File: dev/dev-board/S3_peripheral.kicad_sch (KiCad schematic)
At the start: 0 parts

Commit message: making CAD
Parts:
- added C10, C13, C15, C16, C17, C18, C9: 0.1uF, Capacitor_SMD:C_0603_1608Metric, symbol Device:C
- added C14: 120uF, easyeda2kicad:CAP-SMD_BD8.0-L8.3-W8.3-RD, symbol Device:C_Polarized
- added C19: 10uF, Capacitor_SMD:C_0603_1608Metric, symbol Device:C
- added Card1: TF PUSH, easyeda2kicad:TF-SMD_TF-PUSH, symbol easyeda2kicad:TFPUSH
- added D1: LED GREEN, LED_SMD:LED_0805_2012Metric, symbol Device:LED
- added LED1: TSOP38238, easyeda2kicad:SENSOR-TG_TSOP38236, symbol easyeda2kicad:TSOP38238
- added P1: HDR-IDC-2.54-2X5P, easyeda2kicad:IDC-TH_10P-P2.54_C5665, symbol easyeda2kicad:HDR-IDC-2.54-2X5P
- added R13, R14, R15, R16, R17, R18, R20, R21, R22, R23, R24, R25, R26: 10K, Resistor_SMD:R_0603_1608Metric, symbol Device:R
- added R19: 1K, Resistor_SMD:R_0603_1608Metric, symbol Device:R
- added R27: 22, Resistor_SMD:R_0603_1608Metric, symbol Device:R
- added SW6, SW7, SW8, SW9: TSC015A03526A, easyeda2kicad:SW-SMD_4P-L4.5-W4.5-P3.00-LS6.8, symbol easyeda2kicad:TSC015A03526A
- added U10: TPS2065CDBV, Package_TO_SOT_SMD:SOT-23-5, symbol Power_Management:TPS2065CDBV
- added U11: PESD5V0U2BT, easyeda2kicad:SOT-23-3_L2.9-W1.3-P1.90-LS2.4-BR, symbol easyeda2kicad:PESD5V0U2BT
- added U12: PESD5V0S1BA_C5261083, easyeda2kicad:SOD-323_L1.7-W1.3-LS2.5-BI, symbol easyeda2kicad:PESD5V0S1BA_C5261083
- added U8, U9: ZX-HY2.0-4PWZ, easyeda2kicad:CONN-TH_4P-P2.00_ZX-HY2.0-4PWZ, symbol easyeda2kicad:ZX-HY2.0-4PWZ
- added USB2: USB-231-ARY, easyeda2kicad:USB-A-TH_USB-231-ARY, symbol easyeda2kicad:USB-231-ARY
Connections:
- new net: R18.2, U10.3 (~{FLT})
- new net: D1.2 (A), R19.1
- new net: C14.1, C16.1, U10.1 (OUT), U12.1, USB2.1 (VBUS)
- new net: Card1.5 (CLX), R27.2
- new net +3V3: C17.2, C18.1, C19.1, C9.2, Card1.4 (VDD), LED1.3 (VS), P1.4, R13.2, R14.2, R15.2, R16.2, R20.1, R21.2, R22.2, R23.2, R24.2, R25.1, R26.2
- new net ButtonCancel: R24.1, SW7.1, SW7.2
- new net ButtonDown: R22.1, SW8.1, SW8.2
- new net ButtonEnter: R23.1, SW9.1, SW9.2
- new net ButtonUp: R21.1, SW6.1, SW6.2
- new net GND: C10.1, C13.1, C14.2, C15.1, C16.2, C17.1, C18.2, C19.2, C9.1, Card1.10, Card1.11, Card1.12, Card1.13, Card1.6 (VSS), D1.1 (K), LED1.2 (GND), P1.2, P1.6, P1.9, R17.2, SW6.3, SW6.4, SW7.3, SW7.4, SW8.3, SW8.4, SW9.3, SW9.4, U10.2 (GND), U11.3, U12.2, U8.1, U9.1, USB2.4 (GND), USB2.5 (GND), USB2.6 (GND)
- new net I2C1-SCL: R14.1, U8.4
- new net I2C1-SDA: R13.1, U8.3
- new net I2C2-SCL: R16.1, U9.4
- new net I2C2-SDA: R15.1, U9.3
- new net MTCK: P1.1
- new net MTDI: P1.7
- new net MTDO: P1.3
- new net MTMS: P1.5
- new net RMT: LED1.1 (OUT)
- new net SD-CD: Card1.9 (CD), R26.1
- new net SD-CS0: Card1.2 (CD/DAT3), R25.2
- new net SD-MISO: Card1.7 (DAT0)
- new net SD-MOSI: Card1.3 (CMD), R20.2
- new net SD-SCLK: R27.1
- new net StatLED1: R19.2
- new net USB-D+: U11.1, USB2.3 (D+)
- new net USB-D-: U11.2, USB2.2 (D-)
- new net USB-PWSW: R17.1, U10.4 (EN)
- new net VSYS: C10.2, C13.2, C15.2, R18.1, U10.5 (IN), U8.2, U9.2
- no-connect marks 0 -> 4
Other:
- note added: "左から1"

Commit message: finish cad. 1st step. add symbol,footprint files
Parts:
- D1: LCSC Part (none) -> C2297
- U10: LCSC Part (none) -> C353882
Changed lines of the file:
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@@
+			)
+		)
+		(property "LCSC Part" "C2297"
+			(at 130.81 113.03 0)
+			(effects
+				(font
+					(size 1.27 1.27)
+				)
+				(hide yes)
 			)
 		)
@@
 			(at 60.96 36.83 0)
 			(effects
+				(font
+					(size 1.27 1.27)
+				)
+				(hide yes)
+			)
+		)
+		(property "LCSC Part" "C353882"
+			(at 60.96 36.83 0)
+			(effects

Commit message: complete BOM
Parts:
- added D3: LED RED, LED_SMD:LED_0603_1608Metric, symbol Device:LED
- added R36: 1K, Resistor_SMD:R_0603_1608Metric, symbol Device:R
- C10, C13, C15, C16, C17, C18, C9: LCSC Part (none) -> C14663
- C14: LCSC Part (none) -> C250065
- C19: LCSC Part (none) -> C19702
- R13, R14, R15, R16, R17, R18, R20, R21, R22, R23, R24, R25, R26: LCSC Part (none) -> C25804
- R19: LCSC Part (none) -> C21190
- R27: LCSC Part (none) -> C23345
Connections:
- net GND: now also D3.1 (K)
- net at C14.1, C16.1, U10.1 (OUT)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: now also R36.1
- new net: D3.2 (A), R36.2

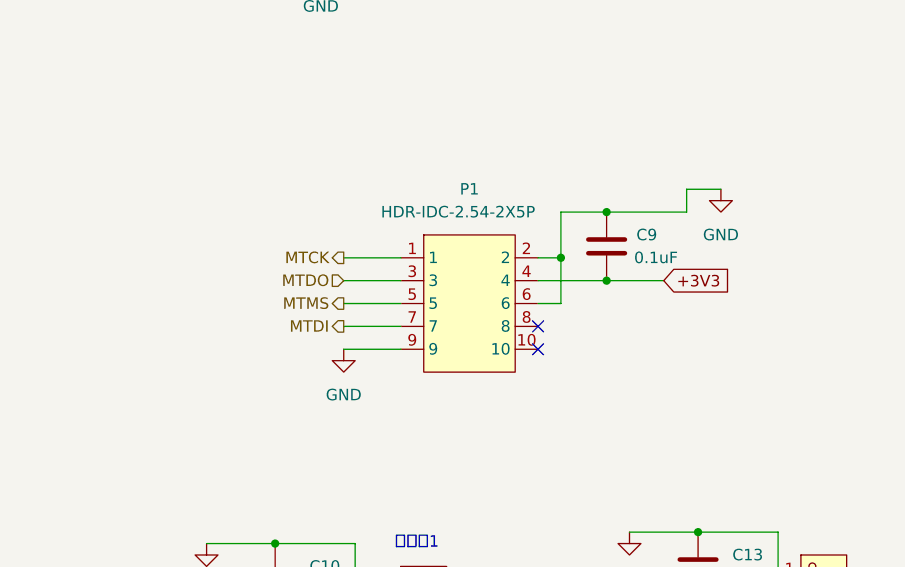
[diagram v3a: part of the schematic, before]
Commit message: change board size. change C14
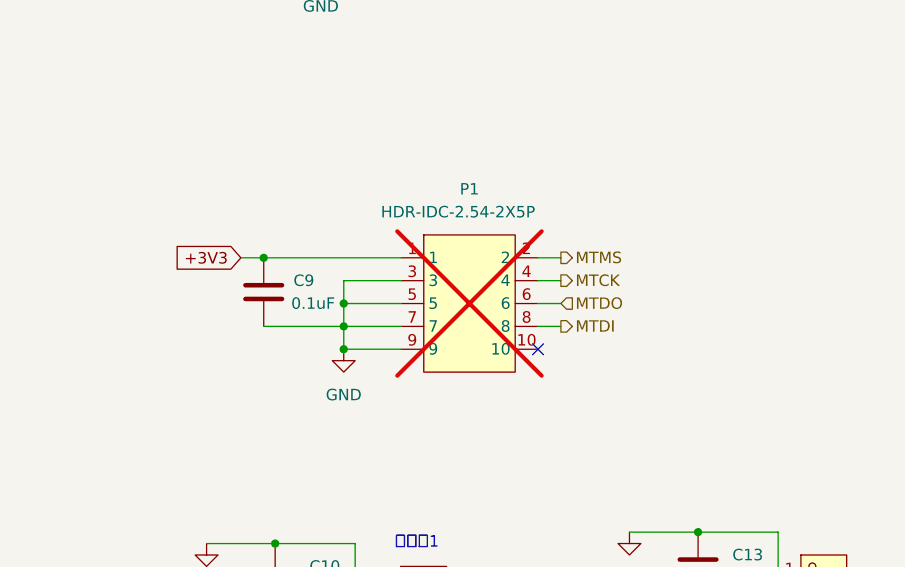
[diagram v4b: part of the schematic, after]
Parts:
- C14: footprint easyeda2kicad:CAP-SMD_BD8.0-L8.3-W8.3-RD -> easyeda2kicad:CAP-SMD_BD6.3-L6.6-W6.6-LS7.2-R-RD
- P1: now not fitted
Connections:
- net +3V3: now also C9.1, P1.1; no longer C9.2, P1.4
- net GND: now also C9.2, P1.3, P1.5, P1.7; no longer C9.1, P1.2, P1.6
- net MTCK: now also P1.4; no longer P1.1
- net MTDI: now also P1.8; no longer P1.7
- net MTDO: now also P1.6; no longer P1.3
- net MTMS: now also P1.2; no longer P1.5
- no-connect marks 4 -> 3
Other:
- moved on the sheet: C9

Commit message: fix LCSC num, improve cad
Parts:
- C14: LCSC Part C250065 -> C250087
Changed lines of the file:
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@@
 			)
 		)
-		(property "LCSC Part" "C250065"
+		(property "LCSC Part" "C250087"
 			(at 77.47 39.37 0)
 			(effects

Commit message: update schematics
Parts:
- removed C17: 0.1uF, Capacitor_SMD:C_0603_1608Metric, symbol Device:C
- removed LED1: TSOP38238, easyeda2kicad:SENSOR-TG_TSOP38236, symbol easyeda2kicad:TSOP38238
- removed SW6, SW7, SW8, SW9: TSC015A03526A, easyeda2kicad:SW-SMD_4P-L4.5-W4.5-P3.00-LS6.8, symbol easyeda2kicad:TSC015A03526A
- added SW5, SW6, SW7, SW8: TS342A2P, easyeda2kicad:KEY-SMD_L3.9-W3.0-LS5.0, symbol easyeda2kicad:TS342A2P160GF021
- R19, R36: value 1K -> 2K; LCSC Part C21190 -> C22975
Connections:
- net ButtonCancel: now also SW6.2
- net ButtonDown: now also SW8.2
- net ButtonEnter: now also SW7.2
- net ButtonUp: now also SW5.2
- net GND: now also SW5.1, SW6.1, SW7.1, SW8.1

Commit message: update for v3r3
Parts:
- added C17, C39: 0.1uF, Capacitor_SMD:C_0603_1608Metric, symbol Device:C
- added D4: LED RED, LED_SMD:LED_0805_2012Metric, symbol Device:LED
- added J1: Conn_01x03_Pin, Connector_PinHeader_2.54mm:PinHeader_1x03_P2.54mm_Vertical, symbol Connector:Conn_01x03_Pin
- added J2: Conn_01x02_Socket, Connector_PinSocket_2.54mm:PinSocket_1x02_P2.54mm_Vertical, symbol Connector:Conn_01x02_Socket
- added R12: 10K, Resistor_SMD:R_0603_1608Metric, symbol Device:R
- added R39, R40, R41: 0, Resistor_SMD:R_0603_1608Metric, symbol Device:R
- added TP1: TestPoint, TestPoint:TestPoint_Pad_D1.0mm, symbol Connector:TestPoint
- added U15: RX8900CE_UB0, easyeda2kicad:SMD-10_L3.2-W2.5-BL_EPSON_RX8900CE, symbol easyeda2kicad:RX8900CE_UB0
- R15: value 10K -> 0; LCSC Part C25804 -> C21189
- R16: value 10K -> 2K; LCSC Part C25804 -> C22975
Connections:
- net +3V3: now also C39.2, J1.3 (Pin_3), R12.1, U15.2 (VDD); no longer R15.2, R16.2
- net GND: now also C17.1, C39.1, D4.1 (K), J2.2 (Pin_2), R41.1, U15.9 (GND)
- net I2C1-SCL: now also U15.5 (SCL)
- net I2C1-SDA: now also U15.7 (SDA)
- net I2C2-SCL: no longer R16.1
- net I2C2-SDA: no longer R15.1
- net MTCK: now also R39.2
- net MTDO: now also R15.2
- net VSYS: now also J1.1 (Pin_1); no longer C13.2, U9.2
- new net: R16.2, R39.1
- new net: R40.1, U15.3 (VBAT)
- new net: C17.2, J2.1 (Pin_1), R40.2
- new net: R12.2, R15.1, U15.10 (~{INT})
- new net: C13.2, J1.2 (Pin_2), U9.2
- new net: D4.2 (A), R16.1
- new net: R41.2, U15.1 (FOE)
- new net: TP1.1, U15.4 (FOUT)
- no-connect marks 3 -> 5
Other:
- moved on the sheet: C10, C13, C9, D1, P1, R13, R14, R19, U8, U9

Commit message: v3 dev r3 candidate2
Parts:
- D4: footprint LED_SMD:LED_0805_2012Metric -> LED_SMD:LED_0603_1608Metric; LCSC Part C2297 -> C2286
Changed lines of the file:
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@@
 			)
 		)
-		(property "Footprint" "LED_SMD:LED_0805_2012Metric"
+		(property "Footprint" "LED_SMD:LED_0603_1608Metric"
 			(at 53.34 87.63 0)
 			(effects
@@
 			)
 		)
-		(property "LCSC Part" "C2297"
+		(property "LCSC Part" "C2286"
 			(at 53.34 87.63 0)
 			(effects
